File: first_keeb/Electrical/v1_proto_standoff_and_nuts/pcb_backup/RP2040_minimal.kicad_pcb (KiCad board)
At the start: 4 copper layers, 67.1 x 66.8 mm, 77 parts, among them J1 Conn_01x04_Socket, P1 USB-TYPE-C-016, Q1 BSS138, SW3 TS-1187A-B-A-B, SW5 TS-1187A-B-A-B, SW6 BUTT1, SW7 BUTT3, SW8 BUTT2, U1 ME6208A44M3G, U2 ME6206A25XG, U3 PRTR5V0U2X, U5 STM32F401RCTx, U7 SLSS49E, U8 SLSS49E, U9 SLSS49E, Y1 8MHz

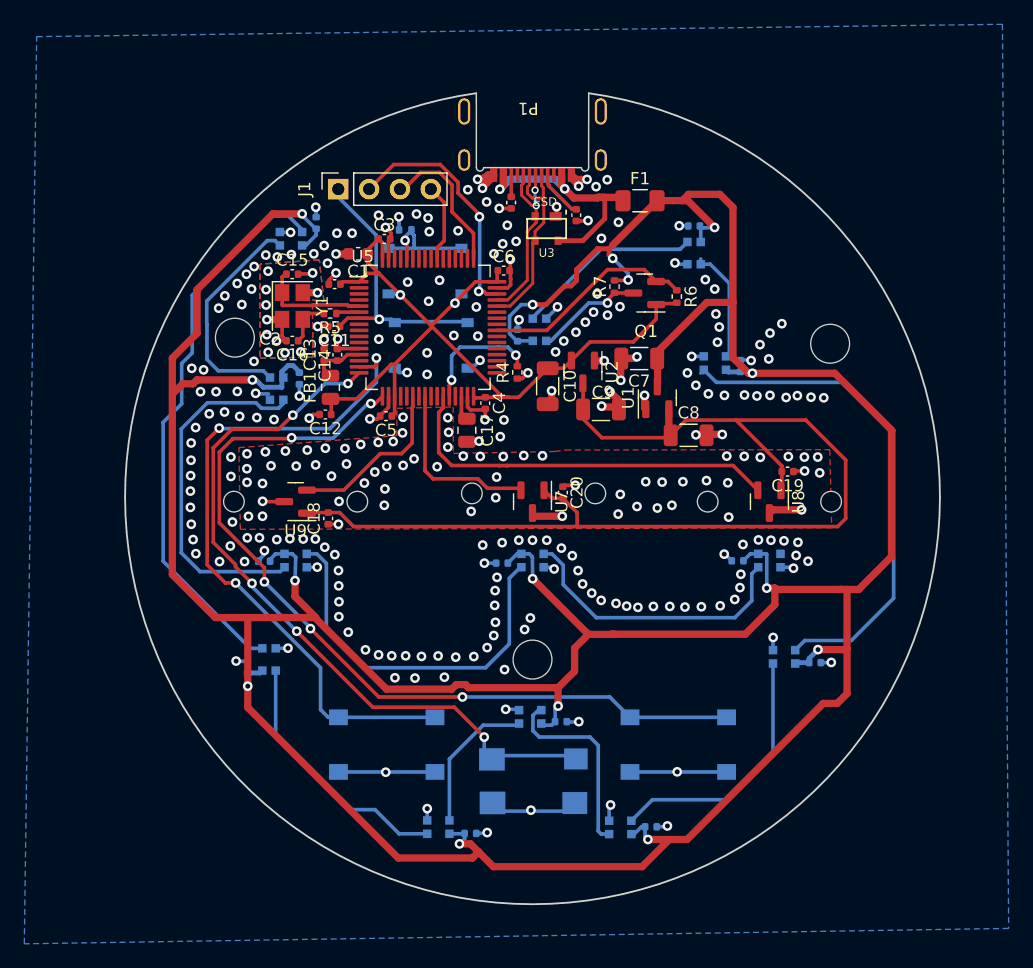
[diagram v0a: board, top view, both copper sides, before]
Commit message: stm fixes, still has different voltages
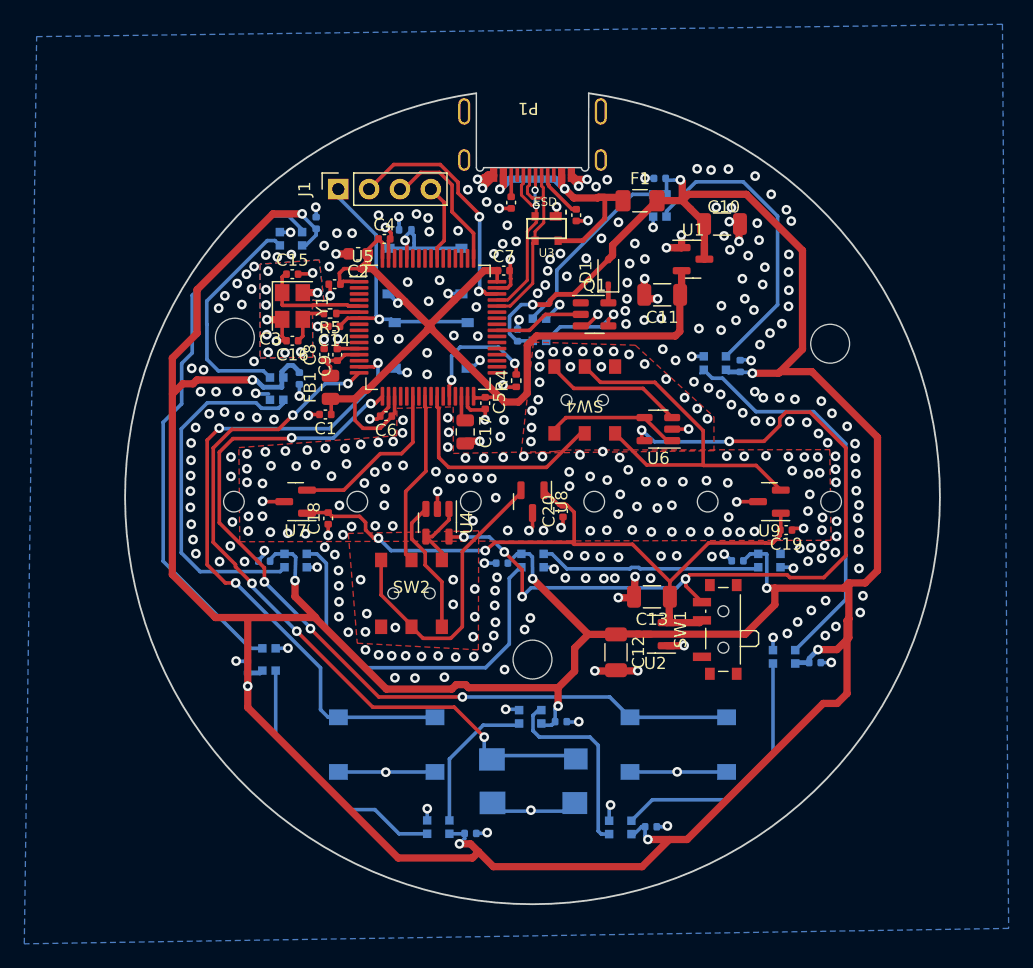
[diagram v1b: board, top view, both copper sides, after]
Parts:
- removed R6, R7: 10k, Resistor_SMD:R_0402_1005Metric
- added D1: 1N4148WS, Diode_SMD:D_SOD-323, F.Cu at (106.2, 81.1)
- added SW1: SK-3296S-01-L3, Button_Switch_SMD:SW_SPDT_PCM12, F.Cu at (115.4, 110.5)
- added SW2: MS-22C01-G010, Button_Switch_SMD:DPDT-MS-22C01, F.Cu at (90.0, 107.5)
- added SW4: MS-22C01-G010, Button_Switch_SMD:DPDT-MS-22C01, F.Cu at (104.3, 91.6)
- added U4: MCP6001-OT, Package_TO_SOT_SMD:SOT-23-5, F.Cu at (92.2, 101.7)
- added U6: MCP6001-OT, Package_TO_SOT_SMD:SOT-23-5, F.Cu at (110.4, 94.0)
- C10: renamed from C9; value 10u -> 22u
- C11: renamed from C10; value 10u -> 22u
- C12: renamed from C7; value 10u -> 22u
- C13: renamed from C8; value 10u -> 22u
- Q1: value BSS138 -> SN74LV1T34DBV; footprint Package_TO_SOT_SMD:SOT-23 -> Package_TO_SOT_SMD:SOT-23-5
- moved C12 24.3 mm to (106.9, 112.4), turned to -90 degrees
- moved U2 19.5 mm to (110.1, 110.9), turned to 180 degrees
- moved C10 18.2 mm to (115.6, 77.2)
- moved C13 13.6 mm to (109.8, 107.8), turned to 180 degrees
- moved U1 13.0 mm to (113.2, 80.0), turned to 0 degrees
- moved C11 12.1 mm to (110.7, 83.0), turned to 180 degrees
- moved C22 4.83 mm to (110.5, 73.4)
- moved D3 4.83 mm to (110.5, 75.6)
- moved C19 4.82 mm to (120.9, 102.3)
- moved Q1 4.49 mm to (105.1, 84.6), turned to 0 degrees
- moved C20 1.53 mm to (102.5, 100.8), turned to 90 degrees
- moved R4 0.69 mm to (98.7, 90.0)
- moved REF** 0.69 mm to (100.0, 100.0)
- moved C17 0.19 mm to (94.5, 94.3)
- turned U9 to 180 degrees
- renumbered C12 to C1, C11 to C14, C1 to C2, C2 to C3, C3 to C4, C4 to C5, C5 to C6, C6 to C7, C13 to C8, C14 to C9, D9 to D10, D10 to D11, D11 to D12, D12 to D13, D13 to D14, D1 to D2, D2 to D3, D3 to D4, D4 to D5, D5 to D6, D6 to D7, D7 to D8, D8 to D9, U2 to U1, U1 to U2, U9 to U7, U7 to U8, U8 to U9
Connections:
- C10 pad 1: +4V4 -> +5V
- D2 pad 3: Net-(D1-DIN) -> Net-(D2-DIN)
- Q1 pad 1: VDD -> unconnected-(Q1-NC-Pad1)
- Q1 pad 3: Net-(D1-DIN) -> GND
- U1 pad 3: +4V4 -> +5V
- U5 pad 26: unconnected-(U5-PB0-Pad26) -> ADC_IN3
- U5 pad 27: ADC_IN3 -> unconnected-(U5-PB1-Pad27)
- U8 pad 2: ADC_IN2 -> S_ADC_IN2
- U9 pad 2: ADC_IN3 -> S_ADC_IN3
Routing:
- net V_test: track 0.00 -> 69.6 mm, vias 0 -> 6
- net +4V4: track 90.2 -> 57.9 mm, vias 0 -> 2
- net S_ADC_IN3: track 0.00 -> 30.4 mm
- net S_ADC_IN2: track 0.00 -> 24.7 mm
- net Net-(D3-DOUT): track 9.57 -> 25.1 mm
- net ADC_IN3: track 32.3 -> 18.7 mm
- net VDD: track 70.9 -> 83.1 mm
- net ALT_ADC_3: track 0.00 -> 11.4 mm
- net ALT_ADC_2: track 0.00 -> 11.2 mm
- net O_ADC_IN3: track 0.00 -> 11.0 mm
- net LED_D: track 17.6 -> 7.44 mm
- net Net-(D1-DIN): track 8.94 -> 0.00 mm, vias 1 -> 0
- net Net-(D4-DOUT): track 41.7 -> 33.3 mm
- net Net-(D2-DIN): track 0.00 -> 7.59 mm, vias 0 -> 1
- net GND: track 113.7 -> 120.6 mm, vias 294 -> 406
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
